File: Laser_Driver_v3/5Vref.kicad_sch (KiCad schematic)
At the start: 14 parts, among them U19 LT3042EDD +5.5V, U4 LM7808_TO220, U6 LTC6655BHLS8-5

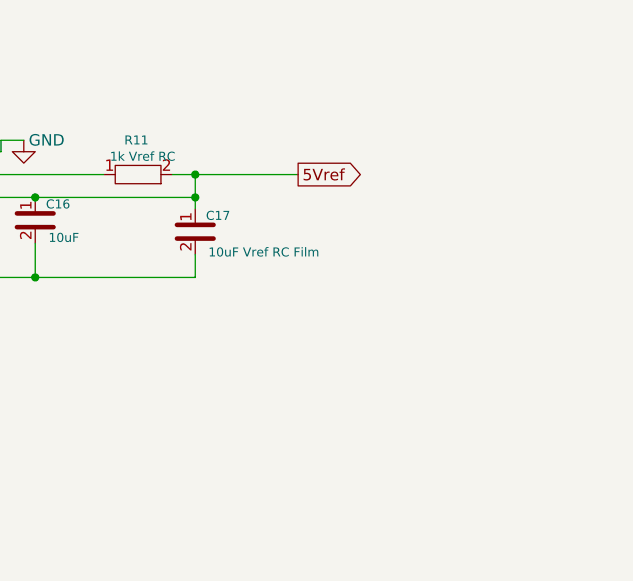
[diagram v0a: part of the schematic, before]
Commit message: Updated 5Vref and TEC and TEC controller
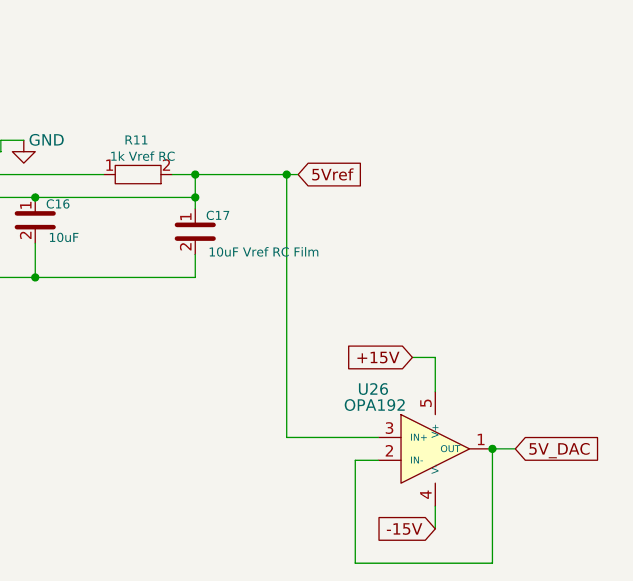
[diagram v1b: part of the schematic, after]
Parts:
- added U26: OPA192, Package_SO:SOIC-5-6_4.4x3.6mm_P1.27mm, symbol Analog:LT1028
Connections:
- net 5Vref: now also U26.3 (IN+)
- new net +15V: U26.5 (V+)
- new net -15V: U26.4 (V-)
- new net 5V_DAC: U26.1 (OUT), U26.2 (IN-)

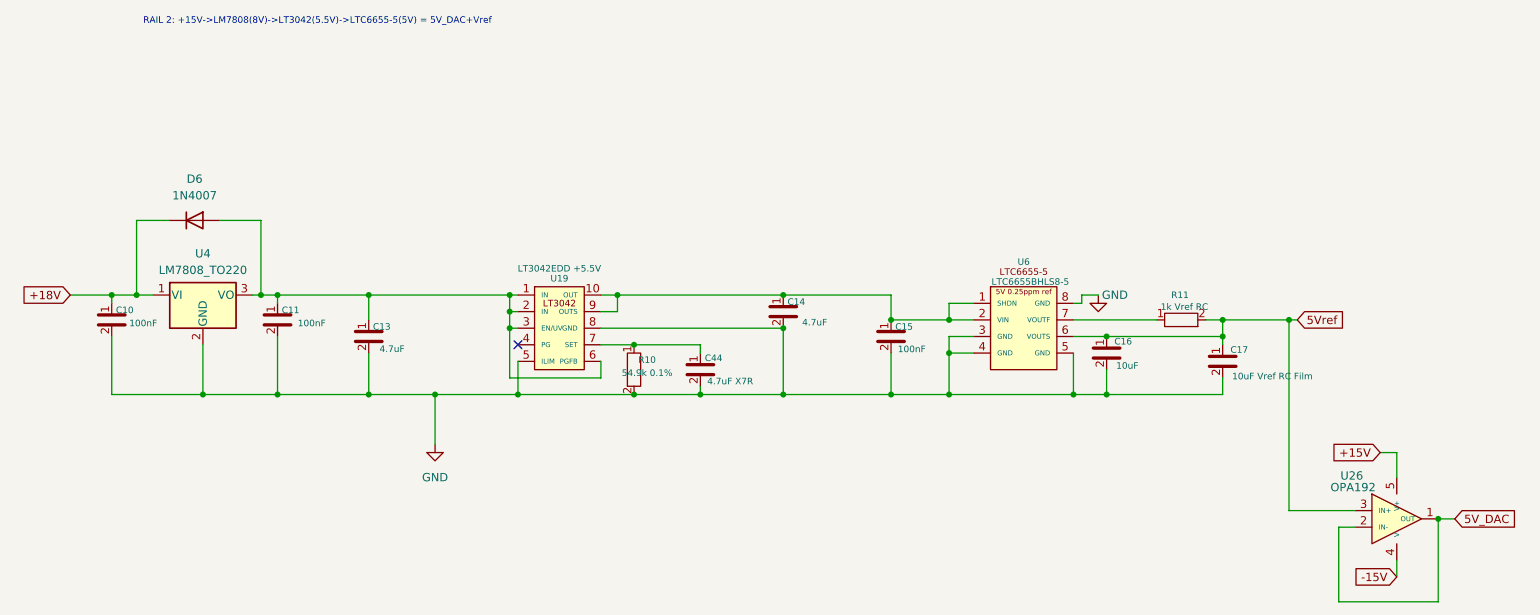
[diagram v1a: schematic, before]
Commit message: Renumbered schematics, corrections, power verified
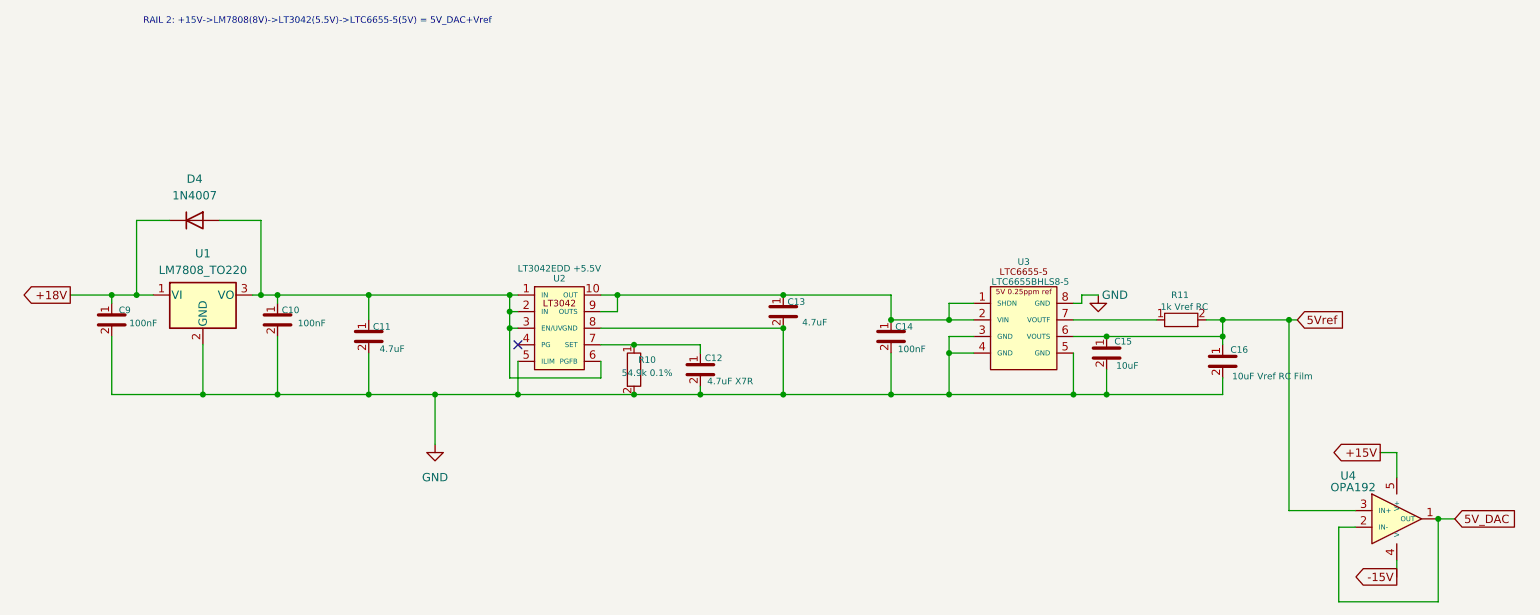
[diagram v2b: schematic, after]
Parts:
- renumbered C11 to C10, C13 to C11, C44 to C12, C14 to C13, C15 to C14, C16 to C15, C17 to C16, C10 to C9, D6 to D4, U4 to U1, U19 to U2, U6 to U3, U26 to U4
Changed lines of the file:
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@@
 	)
 	(global_label "-15V"
-		(shape input)
+		(shape output)
 		(at 250.19 121.92 180)
 		(fields_autoplaced yes)
@@
 	)
 	(global_label "+18V"
-		(shape input)
+		(shape output)
 		(at 46.99 78.74 180)
 		(fields_autoplaced yes)
@@
 	)
 	(global_label "+15V"
-		(shape input)
+		(shape output)
 		(at 247.65 102.87 180)
 		(fields_autoplaced yes)
@@
 		(in_pos_files yes)
 		(dnp no)
-		(property "Reference" "C15"
+		(property "Reference" "C14"
 			(at 174.72 83.59 0)
 			(show_name no)
@@
 			(project "laser_driver_v3"
 				(path "/b2c3d4e5-f6a7-8901-bcde-f12345678901/66b4928b-0f98-4282-b6fa-f46162bb9680"
-					(reference "C15")
+					(reference "C14")
 					(unit 1)
 				)
@@
 		(in_pos_files yes)
 		(dnp no)
-		(property "Reference" "C11"
+		(property "Reference" "C10"
 			(at 80.74 81.05 0)
 			(show_name no)
@@
 			(project "laser_driver_v3"
 				(path "/b2c3d4e5-f6a7-8901-bcde-f12345678901/66b4928b-0f98-4282-b6fa-f46162bb9680"
-					(reference "C11")
+					(reference "C10")
 					(unit 1)
 				)
@@
 		(in_pos_files yes)
 		(dnp no)
-		(property "Reference" "C16"
+		(property "Reference" "C15"
 			(at 208.28 85.852 0)
 			(show_name no)
@@
 			(project "laser_driver_v3"
 				(path "/b2c3d4e5-f6a7-8901-bcde-f12345678901/66b4928b-0f98-4282-b6fa-f46162bb9680"
-					(reference "C16")
+					(reference "C15")
 					(unit 1)
 				)
@@
 		(dnp no)
 		(fields_autoplaced yes)
-		(property "Reference" "#PWR03"
+		(property "Reference" "#PWR05"
 			(at 102.87 107.95 0)
 			(hide yes)
@@
 			(project "laser_driver_v3"
 				(path "/b2c3d4e5-f6a7-8901-bcde-f12345678901/66b4928b-0f98-4282-b6fa-f46162bb9680"
-					(reference "#PWR03")
+					(reference "#PWR05")
 					(unit 1)
 				)
@@
 		(in_pos_files yes)
 		(dnp no)
-		(property "Reference" "C13"
+		(property "Reference" "C11"
 			(at 94.71 83.59 0)
 			(show_name no)
@@
 			(project "laser_driver_v3"
 				(path "/b2c3d4e5-f6a7-8901-bcde-f12345678901/66b4928b-0f98-4282-b6fa-f46162bb9680"
-					(reference "C13")
+					(reference "C11")
 					(unit 1)
 				)
@@
 		(dnp no)
 		(fields_autoplaced yes)
-		(property "Reference" "U4"
+		(property "Reference" "U1"
 			(at 67.31 72.39 0)
 			(show_name no)
@@
 			(project "laser_driver_v3"
 				(path "/b2c3d4e5-f6a7-8901-bcde-f12345678901/66b4928b-0f98-4282-b6fa-f46162bb9680"
-					(reference "U4")
+					(reference "U1")
 					(unit 1)
 				)
@@
 		(in_pos_files yes)
 		(dnp no)
-		(property "Reference" "C17"
+		(property "Reference" "C16"
 			(at 226.06 87.122 0)
 			(show_name no)
@@
 			(project "laser_driver_v3"
 				(path "/b2c3d4e5-f6a7-8901-bcde-f12345678901/66b4928b-0f98-4282-b6fa-f46162bb9680"
-					(reference "C17")
+					(reference "C16")
 					(unit 1)
 				)
@@
 		(in_pos_files yes)
 		(dnp no)
-		(property "Reference" "C14"
+		(property "Reference" "C13"
 			(at 158.21 79.78 0)
 			(show_name no)
@@
 			(project "laser_driver_v3"
 				(path "/b2c3d4e5-f6a7-8901-bcde-f12345678901/66b4928b-0f98-4282-b6fa-f46162bb9680"
-					(reference "C14")
+					(reference "C13")
 					(unit 1)
 				)
@@
 		(in_pos_files yes)
 		(dnp no)
-		(property "Reference" "C10"
+		(property "Reference" "C9"
 			(at 55.34 81.05 0)
 			(show_name no)
@@
 			(project "laser_driver_v3"
 				(path "/b2c3d4e5-f6a7-8901-bcde-f12345678901/66b4928b-0f98-4282-b6fa-f46162bb9680"
-					(reference "C10")
+					(reference "C9")
 					(unit 1)
 				)
@@
 		(in_pos_files yes)
 		(dnp no)
-		(property "Reference" "C44"
+		(property "Reference" "C12"
 			(at 145.542 88.392 0)
 			(show_name no)
@@
 			(project "laser_driver_v3"
 				(path "/b2c3d4e5-f6a7-8901-bcde-f12345678901/66b4928b-0f98-4282-b6fa-f46162bb9680"
-					(reference "C44")
+					(reference "C12")
 					(unit 1)
 				)
@@
 		(in_pos_files yes)
 		(dnp no)
-		(property "Reference" "U6"
+		(property "Reference" "U3"
 			(at 193.04 73.66 0)
 			(show_name no)
@@
 			(project "laser_driver_v3"
 				(path "/b2c3d4e5-f6a7-8901-bcde-f12345678901/66b4928b-0f98-4282-b6fa-f46162bb9680"
-					(reference "U6")
+					(reference "U3")
 					(unit 1)
 				)
@@
 		(dnp no)
 		(fields_autoplaced yes)
-		(property "Reference" "D6"
+		(property "Reference" "D4"
 			(at 66.04 60.96 0)
 			(show_name no)
@@
 			(project "laser_driver_v3"
 				(path "/b2c3d4e5-f6a7-8901-bcde-f12345678901/66b4928b-0f98-4282-b6fa-f46162bb9680"
-					(reference "D6")
+					(reference "D4")
 					(unit 1)
 				)
@@
 		(in_pos_files yes)
 		(dnp no)
-		(property "Reference" "U19"
+		(property "Reference" "U2"
 			(at 121.92 76.2 0)
 			(show_name no)
@@
 			(project "laser_driver_v3"
 				(path "/b2c3d4e5-f6a7-8901-bcde-f12345678901/66b4928b-0f98-4282-b6fa-f46162bb9680"
-					(reference "U19")
+					(reference "U2")
 					(unit 1)
 				)
@@
 		(in_pos_files yes)
 		(dnp no)
-		(property "Reference" "#PWR05"
+		(property "Reference" "#PWR06"
 			(at 204.47 85.09 0)
 			(hide yes)
@@
 			(project "laser_driver_v3"
 				(path "/b2c3d4e5-f6a7-8901-bcde-f12345678901/66b4928b-0f98-4282-b6fa-f46162bb9680"
-					(reference "#PWR05")
+					(reference "#PWR06")
 					(unit 1)
 				)
@@
 		(in_pos_files yes)
 		(dnp no)
-		(property "Reference" "U26"
+		(property "Reference" "U4"
 			(at 241.554 106.426 0)
 			(show_name no)
@@
 			(project "laser_driver_v3"
 				(path "/b2c3d4e5-f6a7-8901-bcde-f12345678901/66b4928b-0f98-4282-b6fa-f46162bb9680"
-					(reference "U26")
-					(unit 1)
-				)
+					(reference "U4")
+					(unit 1)
+				)

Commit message: Update names, footprints, values, and created BOM
Updated files names, foot prints, component values, parts.
Assigned values from Digikey catalog.
Created CSV BOMs for each schematic.
Including a Power analysis now for all components.
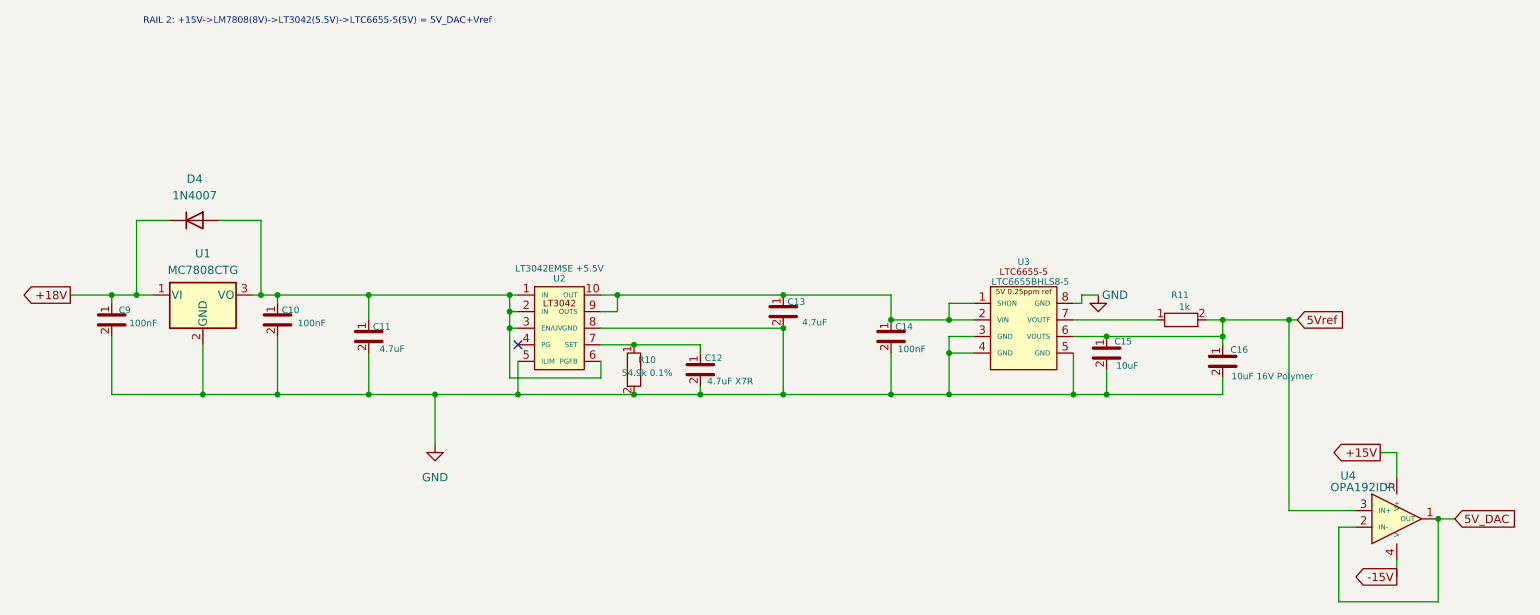
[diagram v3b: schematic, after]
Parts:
- C16: value 10uF Vref RC Film -> 10uF 16V Polymer; footprint Capacitor_SMD:C_0805_2012Metric_Pad1.18x1.45mm_HandSolder -> Capacitor_THT:CP_Radial_D4.0mm_P2.00mm
- R10: footprint Resistor_SMD:R_0402_1005Metric -> Resistor_SMD:R_0805_2012Metric_Pad1.20x1.40mm_HandSolder
- R11: value 1k Vref RC -> 1k; footprint Resistor_SMD:R_0402_1005Metric -> Resistor_SMD:R_0805_2012Metric_Pad1.20x1.40mm_HandSolder
- U1: value LM7808_TO220 -> MC7808CTG
- U2: value LT3042EDD +5.5V -> LT3042EMSE +5.5V; footprint Package_DFN_QFN:DFN-10-1EP_3x3mm_P0.5mm_EP1.65x2.38mm -> Package_SO:MSOP-16_3x5mm_P0.65mm
- U4: value OPA192 -> OPA192IDR; footprint Package_SO:SOIC-5-6_4.4x3.6mm_P1.27mm -> Package_SO:SOIC-8_3.9x4.9mm_P1.27mm
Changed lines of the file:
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@@
 			)
 		)
-		(property "Value" "LM7808_TO220"
+		(property "Value" "MC7808CTG"
 			(at 67.31 74.93 0)
 			(show_name no)
@@
 			)
 		)
-		(property "Value" "10uF Vref RC Film"
+		(property "Value" "10uF 16V Polymer"
 			(at 231.14 91.186 0)
 			(show_name no)
@@
 			)
 		)
-		(property "Footprint" "Capacitor_SMD:C_0805_2012Metric_Pad1.18x1.45mm_HandSolder"
+		(property "Footprint" "Capacitor_THT:CP_Radial_D4.0mm_P2.00mm"
 			(at 75.52 60.9 0)
 			(hide yes)
@@
 			)
 		)
-		(property "Footprint" "Resistor_SMD:R_0402_1005Metric"
+		(property "Footprint" "Resistor_SMD:R_0805_2012Metric_Pad1.20x1.40mm_HandSolder"
 			(at 60.35 58.17 0)
 			(hide yes)
@@
 			)
 		)
-		(property "Value" "LT3042EDD +5.5V"
+		(property "Value" "LT3042EMSE +5.5V"
 			(at 121.92 74.676 0)
 			(show_name no)
@@
 			)
 		)
-		(property "Footprint" "Package_DFN_QFN:DFN-10-1EP_3x3mm_P0.5mm_EP1.65x2.38mm"
+		(property "Footprint" "Package_SO:MSOP-16_3x5mm_P0.65mm"
 			(at 41.92 60.55 0)
 			(hide yes)
@@
 			)
 		)
-		(property "Value" "1k Vref RC"
+		(property "Value" "1k"
 			(at 217.67 80.55 90)
 			(show_name no)
@@
 			)
 		)
-		(property "Footprint" "Resistor_SMD:R_0402_1005Metric"
+		(property "Footprint" "Resistor_SMD:R_0805_2012Metric_Pad1.20x1.40mm_HandSolder"
 			(at 195.17 222.55 0)
 			(hide yes)
@@
 			)
 		)
-		(property "Value" "OPA192"
+		(property "Value" "OPA192IDR"
 			(at 240.03 108.204 0)
 			(show_name no)
@@
 			)
 		)
-		(property "Footprint" "Package_SO:SOIC-5-6_4.4x3.6mm_P1.27mm"
+		(property "Footprint" "Package_SO:SOIC-8_3.9x4.9mm_P1.27mm"
 			(at 255.016 95.504 0)
 			(hide yes)

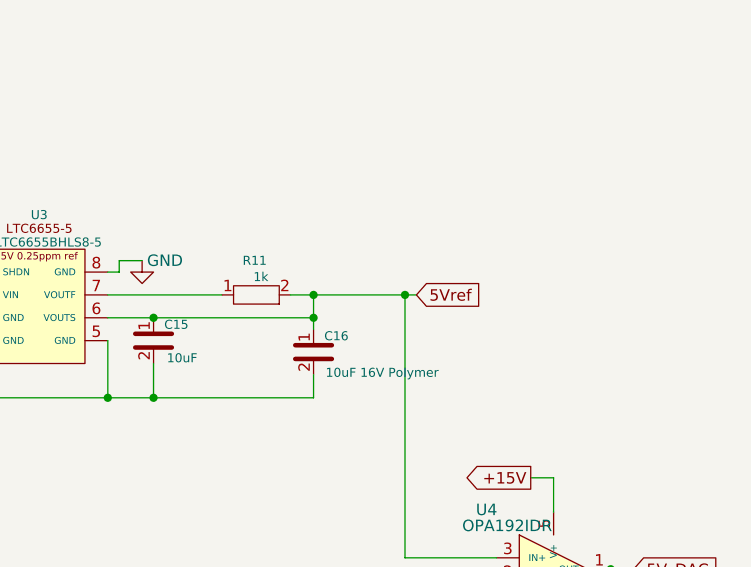
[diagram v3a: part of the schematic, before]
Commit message: Clearing ERC errors. laying out components.
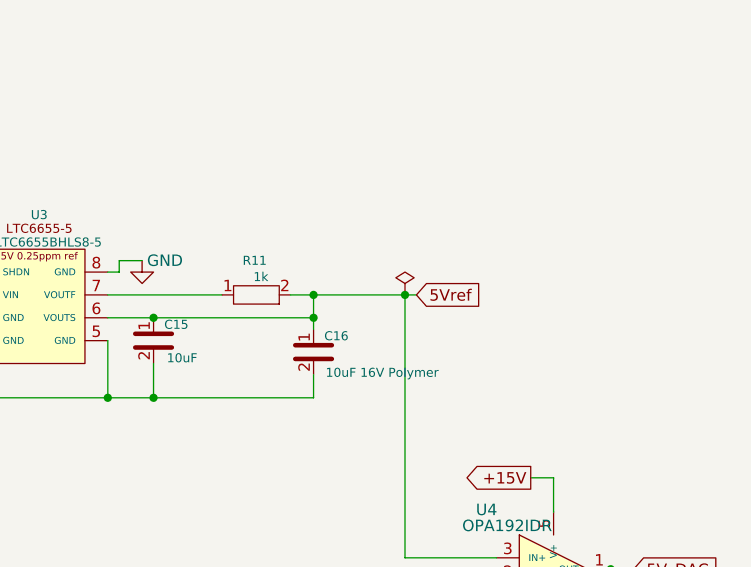
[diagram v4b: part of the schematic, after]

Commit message: Update to teensy pinout and config. Working on PCB
Improved pin selection on Teensy for better operation.
Started working through the PCB from in the power input.
Updating footprints and getting the layout organized.
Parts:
- U2: footprint Package_SO:MSOP-16_3x5mm_P0.65mm -> Package_SO:MSOP-10-1EP_3x3mm_P0.5mm_EP2.2x3.1mm_Mask1.83x1.89mm_ThermalVias
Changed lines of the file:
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@@
 			)
 		)
-		(property "Footprint" "Package_SO:MSOP-16_3x5mm_P0.65mm"
+		(property "Footprint" "Package_SO:MSOP-10-1EP_3x3mm_P0.5mm_EP2.2x3.1mm_Mask1.83x1.89mm_ThermalVias"
 			(at 41.92 60.55 0)
 			(hide yes)

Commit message: Working through power supply layout and footprints
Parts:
- D4: footprint Diode_THT:D_DO-41_SOD81_P10.16mm_Horizontal -> Diode_THT:D_DO-15_P12.70mm_Horizontal
- U3: footprint Package_SO:SOIC-8_3.9x4.9mm_P1.27mm -> Package_SO:MSOP-8_3x3mm_P0.65mm
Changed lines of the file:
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@@
 			)
 		)
-		(property "Footprint" "Package_SO:SOIC-8_3.9x4.9mm_P1.27mm"
+		(property "Footprint" "Package_SO:MSOP-8_3x3mm_P0.65mm"
 			(at 73.04 60.55 0)
 			(hide yes)
@@
 			)
 		)
-		(property "Datasheet" ""
+		(property "Datasheet" "https://www.analog.com/media/en/technical-documentation/data-sheets/ltc6655-6655ln.pdf"
 			(at 73.04 60.55 0)
 			(hide yes)
@@
 			)
 		)
-		(property "Footprint" "Diode_THT:D_DO-41_SOD81_P10.16mm_Horizontal"
+		(property "Footprint" "Diode_THT:D_DO-15_P12.70mm_Horizontal"
 			(at 66.04 71.755 0)
 			(hide yes)

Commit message: Many changes.  Working through ERC.
Main changes are for the grounds.  I found the NETTIE function to tie the GND, DGND and AGND together at a specific point on the boud with a footprint even.
Changed transformers one more time to be consistent for both.
Updated footprints to be consistent and avoid power input/output errors with the ERC.
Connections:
- net +18V renamed +22V
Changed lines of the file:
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@@
 		)
 	)
-	(global_label "+18V"
+	(global_label "+22V"
 		(shape output)
 		(at 46.99 78.74 180)
